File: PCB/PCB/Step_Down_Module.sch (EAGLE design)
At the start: 48 parts, among them J1 JUMPER-SMT_3_1-NC_PASTE_SILK, J2 JUMPER-SMT_3_1-NC_PASTE_SILK, J7 JUMPER-SMT_3_1-NC_PASTE_SILK, Q1 FDMC86240, Q2 FDMC86240, Q3 TPH2900ENH, U1 LTC3895_STEP_DOWN_DC-DC_CONVE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

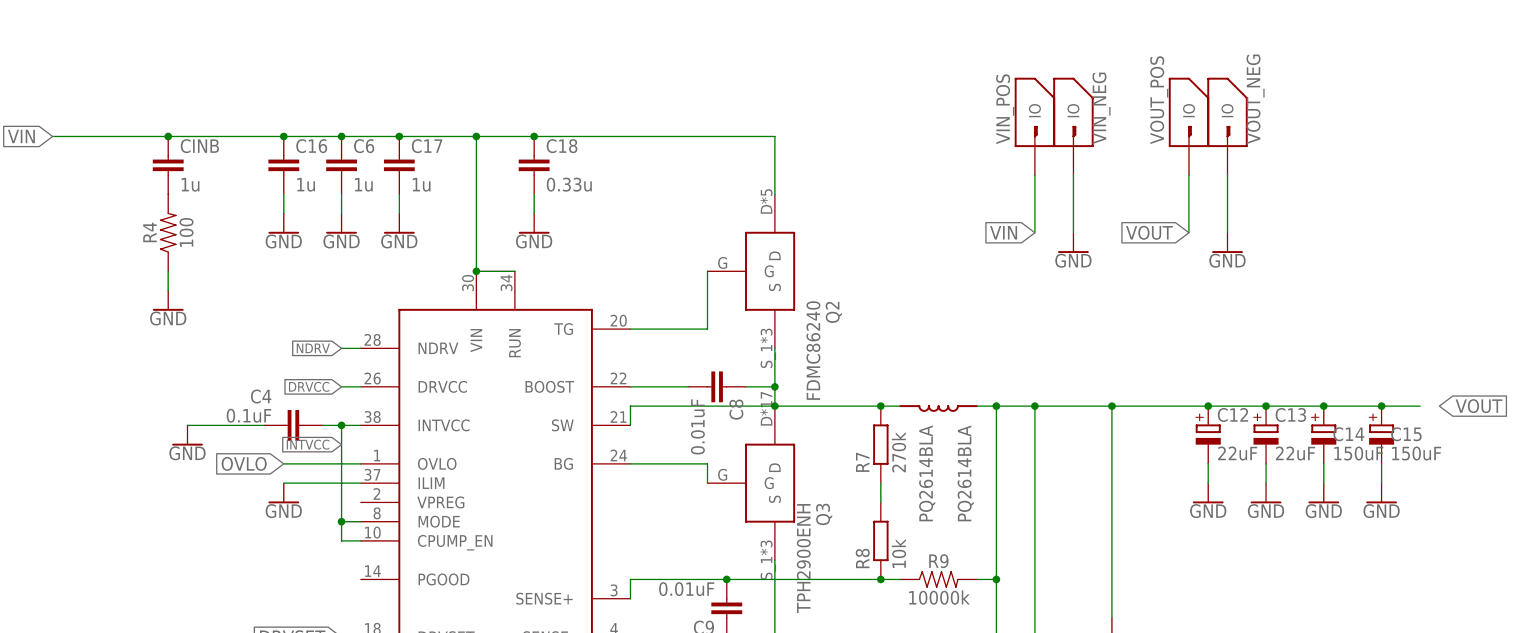
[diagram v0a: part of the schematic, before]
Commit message: WIP-PCB revision 2; Major parts of layout done
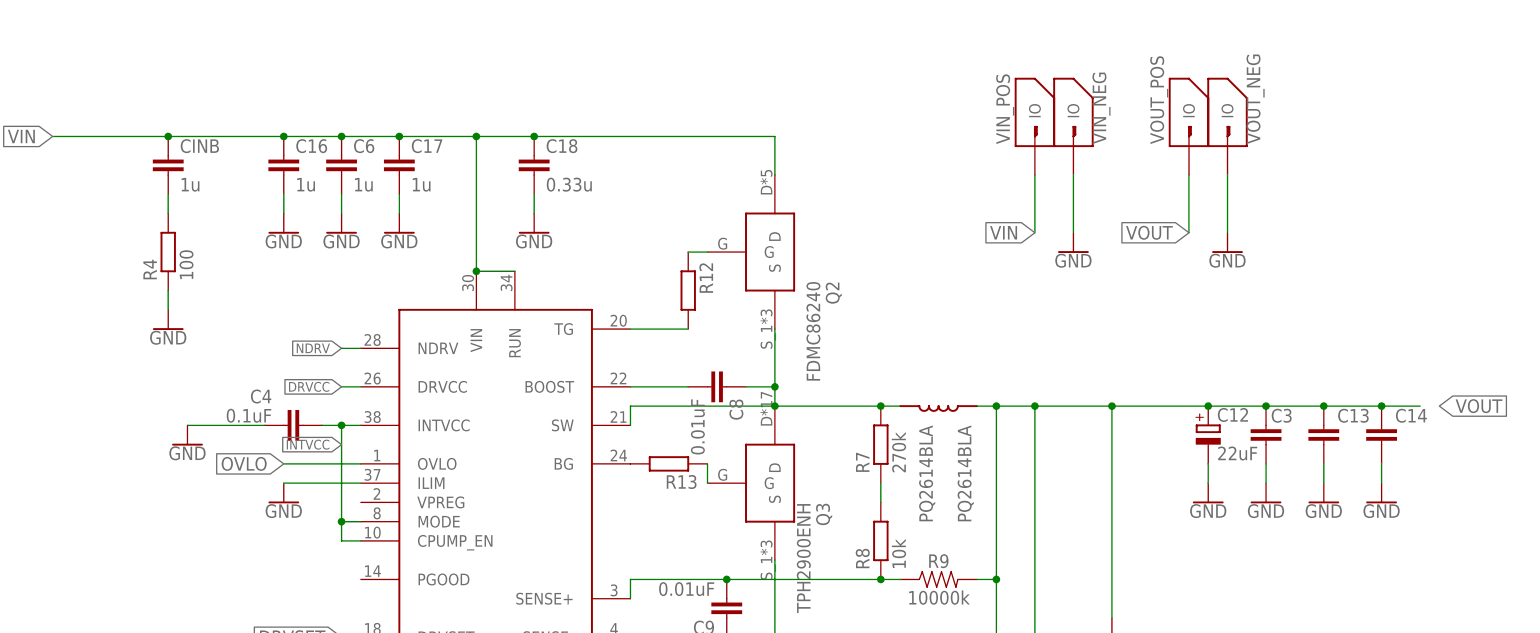
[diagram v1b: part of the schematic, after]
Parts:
- removed C15: 150uF, rcl:CPOL-EUE5-10.5
- added C3: (no value), rcl:C-EUC0805
- added R12, R13: (no value), rcl:R-EU_R0805
- C13: value 22uF -> (none); device rcl:CPOL-EUE5-5 -> rcl:C-EUC0805
- C14: value 150uF -> (none); device rcl:CPOL-EUE5-10.5 -> rcl:C-EUC0805
- R4: device SparkFun-Resistors:RESISTORAXIAL-0.3 -> resistor:R-EU_0204/5
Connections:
- new net N$2: Q2.G, R12.1
- new net N$3: Q3.G, R13.1
- net G2: now also R12.2; no longer Q2.G
- net G3: now also R13.2; no longer Q3.G
- net GND: now also C13.2, C14.2, C3.2; no longer C13.-, C14.-, C15.-
- net VOUT: now also C13.1, C14.1, C3.1; no longer C13.+, C14.+, C15.+
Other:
- moved on the sheet: Q2

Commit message: WIP:PCB revision 2; Move inductor and optimize SW Node area
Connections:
- net N$6 renamed S+
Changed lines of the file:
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@@
 <part name="VIN_POS" library="IO_pad" deviceset="IO_PAD_SINGLE" device=""/>
 <part name="VIN_NEG" library="IO_pad" deviceset="IO_PAD_SINGLE" device=""/>
-<part name="VOUT_POS" library="IO_pad" deviceset="IO_PAD_SINGLE" device=""/>
 <part name="VOUT_NEG" library="IO_pad" deviceset="IO_PAD_SINGLE" device=""/>
 <part name="U$1" library="IO_pad" deviceset="CONN_VIA" device=""/>
@@
 <part name="C13" library="rcl" library_urn="urn:adsk.eagle:library:334" deviceset="C-EU" device="C0805" package3d_urn="urn:adsk.eagle:package:23617/2"/>
 <part name="C14" library="rcl" library_urn="urn:adsk.eagle:library:334" deviceset="C-EU" device="C0805" package3d_urn="urn:adsk.eagle:package:23617/2"/>
+<part name="VOUT_POS" library="IO_pad" deviceset="IO_PAD_SINGLE" device=""/>
 </parts>
 <sheets>
@@
 <attribute name="NAME" x="100.838" y="108.204" size="1.778" layer="95" rot="R90"/>
 </instance>
-<instance part="VOUT_POS" gate="G$1" x="109.22" y="111.76" smashed="yes">
-<attribute name="NAME" x="108.458" y="108.204" size="1.778" layer="95" rot="R90"/>
-</instance>
 <instance part="VOUT_NEG" gate="G$1" x="114.3" y="111.76" smashed="yes">
 <attribute name="NAME" x="121.158" y="108.204" size="1.778" layer="95" rot="R90"/>
@@
 <attribute name="NAME" x="143.256" y="73.279" size="1.778" layer="95" rot="R180"/>
 <attribute name="VALUE" x="139.319" y="72.644" size="1.778" layer="96" rot="R90"/>
+</instance>
+<instance part="VOUT_POS" gate="G$1" x="109.22" y="111.76" smashed="yes">
+<attribute name="NAME" x="108.458" y="108.204" size="1.778" layer="95" rot="R90"/>
 </instance>
 </instances>
@@
 </segment>
 </net>
-<net name="N$6" class="0">
+<net name="S+" class="0">
 <segment>
 <pinref part="U1" gate="G$1" pin="SENSE+"/>

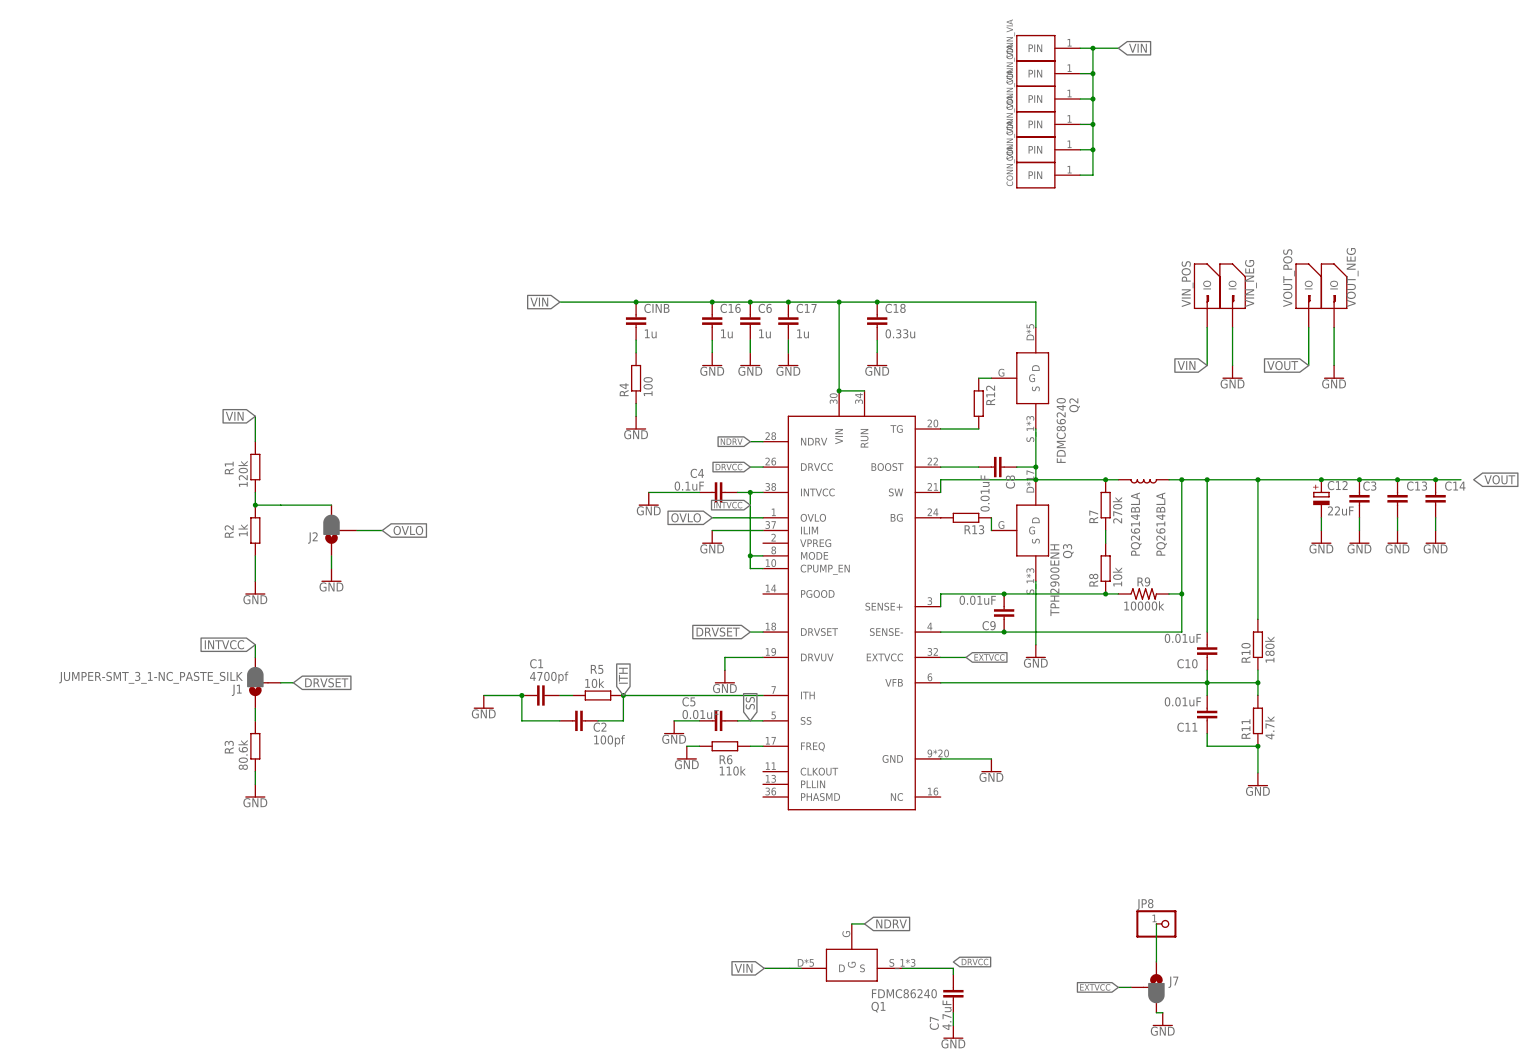
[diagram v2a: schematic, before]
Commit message: Corrected sense resistors, DRVCC trace
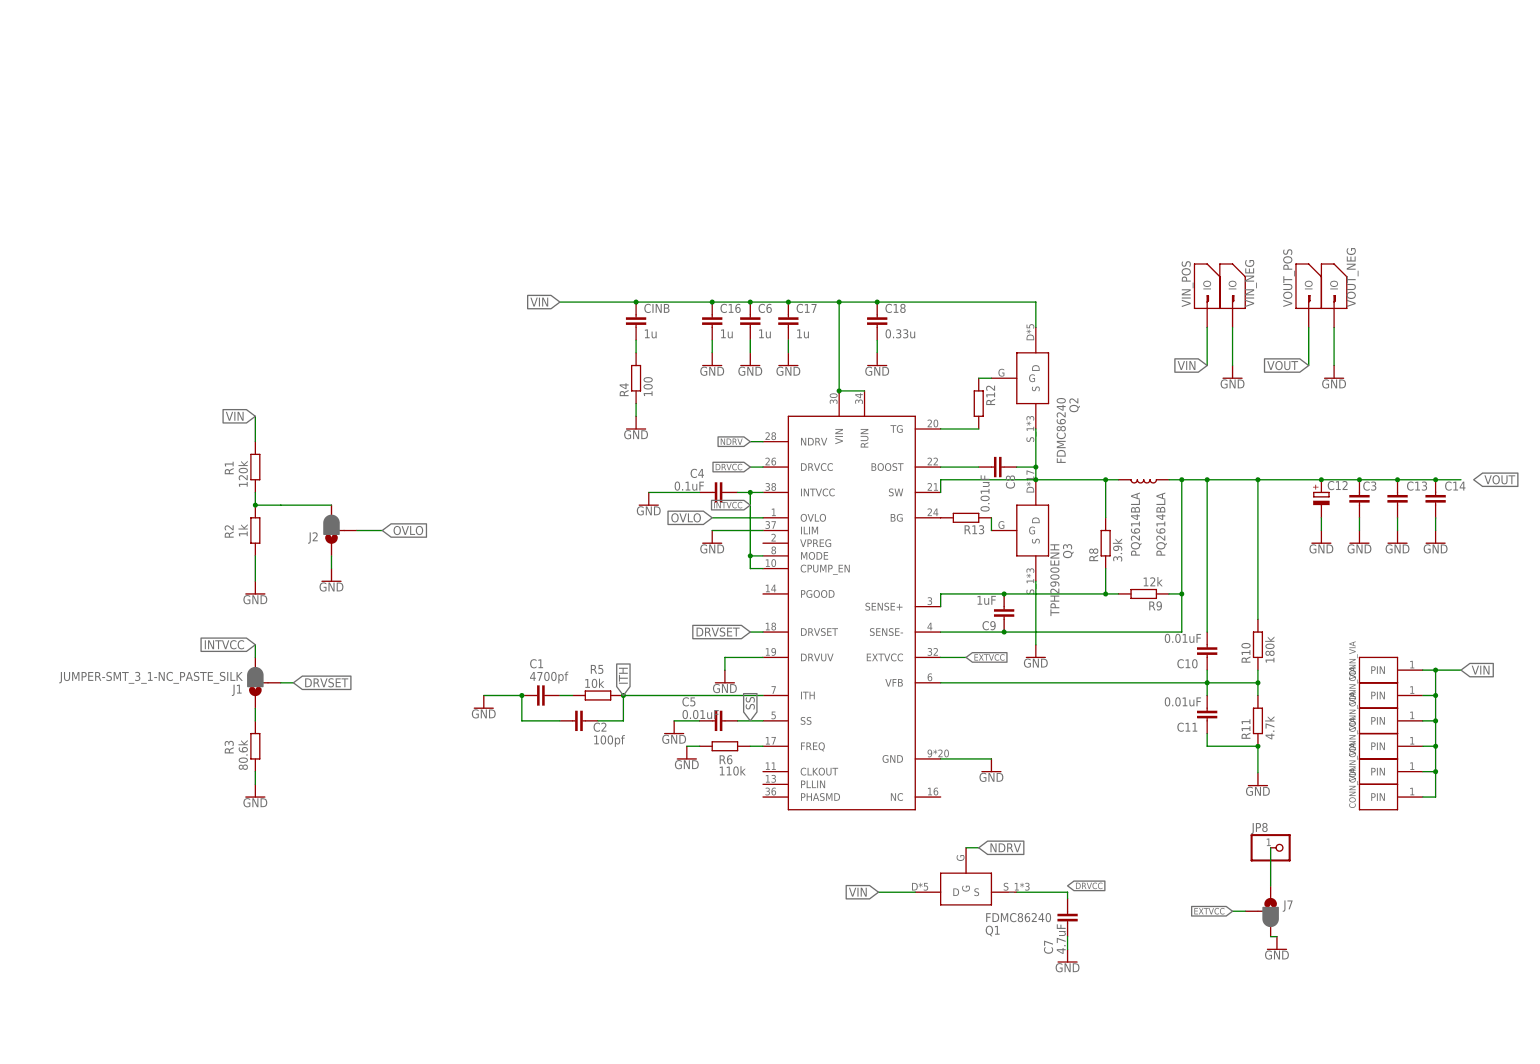
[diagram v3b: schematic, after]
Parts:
- removed R7: 270k, rcl:R-EU_R0805
- C12: value 22uF -> (none)
- C9: value 0.01uF -> 1uF
- R8: value 10k -> 3.9k; device rcl:R-EU_R0805 -> resistor:R-EU_0204/5
- R9: value 10000k -> 12k; device SparkFun-Resistors:RESISTORAXIAL-0.3 -> resistor:R-EU_0204/5
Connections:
- removed net N$7: R7.1, R8.2
- net S+: now also R9.2; no longer R9.1
- net SW: now also R8.2; no longer R7.2
- net VOUT: now also R9.1; no longer R9.2
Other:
- moved on the sheet: C7, J7, JP8, Q1, R8

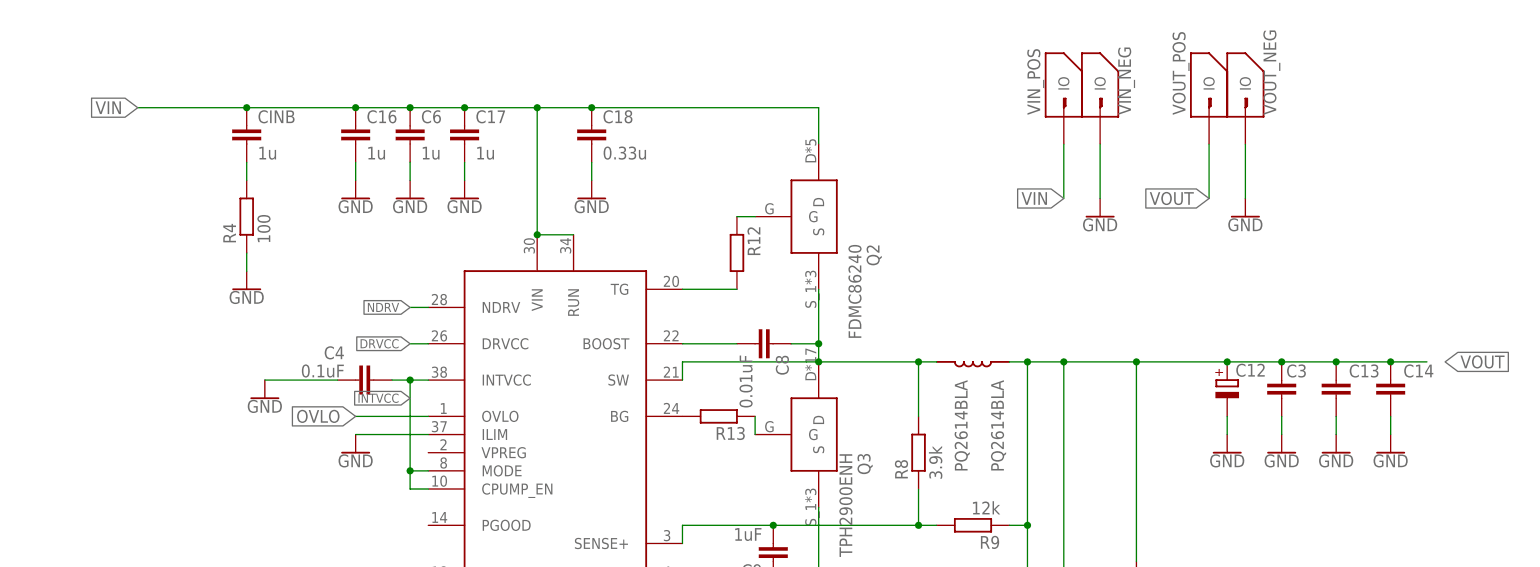
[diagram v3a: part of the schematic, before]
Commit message: Added electrolytics, test points
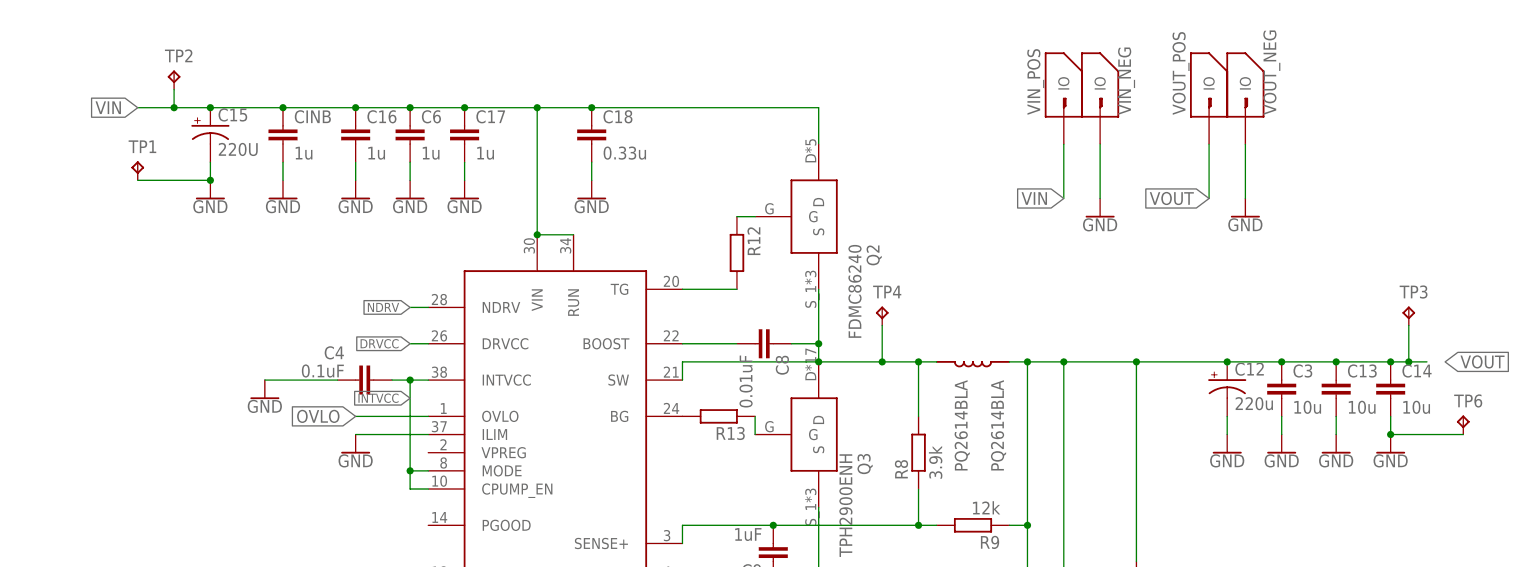
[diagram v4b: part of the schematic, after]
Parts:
- removed R4: 100, resistor:R-EU_0204/5
- added C15: 220U, SparkFun-Capacitors:220U
- added TP1, TP2, TP3, TP4, TP6: TPTP16R, testpad:TPTP16R
- C12: value (none) -> 220u; device rcl:CPOL-EUE5-5 -> SparkFun-Capacitors:1000UF-RADIAL-5MM-25V-20%
- C13, C14, C3: value (none) -> 10u; device rcl:C-EUC0805 -> SparkFun-Capacitors:CAP_SMD_1210
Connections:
- removed net N$1: CINB.2, R4.2
- net GND: now also C15.-, CINB.2, TP1.TP, TP6.TP; no longer R4.1
- net SW: now also TP4.TP
- net VIN: now also C15.+, TP2.TP
- net VOUT: now also TP3.TP
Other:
- moved on the sheet: CINB

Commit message: PCB rev2 sent for manufacture
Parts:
- added C19: 10u, SparkFun-Capacitors:CAP_SMD_1210
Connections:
- net GND: now also C19.2
- net VOUT: now also C19.1
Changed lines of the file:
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@@
 <part name="TP4" library="testpad" library_urn="urn:adsk.eagle:library:385" deviceset="TP" device="TP16R" package3d_urn="urn:adsk.eagle:package:27969/1"/>
 <part name="TP6" library="testpad" library_urn="urn:adsk.eagle:library:385" deviceset="TP" device="TP16R" package3d_urn="urn:adsk.eagle:package:27969/1"/>
+<part name="C19" library="SparkFun-Capacitors" deviceset="CAP_SMD_1210" device="" value="10u"/>
+<part name="GND28" library="SparkFun-PowerSymbols" library_urn="urn:adsk.eagle:library:530" deviceset="GND" device=""/>
 </parts>
 <sheets>
@@
 <attribute name="NAME" x="146.05" y="67.31" size="1.778" layer="95"/>
 <attribute name="TP_SIGNAL_NAME" x="148.59" y="64.77" size="1.778" layer="97"/>
+</instance>
+<instance part="C19" gate="G$1" x="121.92" y="78.74" smashed="yes" rot="R180">
+<attribute name="NAME" x="120.396" y="75.819" size="1.778" layer="95" font="vector" rot="R180"/>
+<attribute name="VALUE" x="120.396" y="80.899" size="1.778" layer="96" font="vector" rot="R180"/>
+</instance>
+<instance part="GND28" gate="1" x="121.92" y="86.36" smashed="yes" rot="R180">
+<attribute name="VALUE" x="121.92" y="86.614" size="1.778" layer="96" rot="R180" align="top-center"/>
 </instance>
 </instances>
@@
 <wire x1="139.7" y1="78.74" x2="139.7" y2="73.66" width="0.1524" layer="91"/>
 <junction x="139.7" y="73.66"/>
+<pinref part="C19" gate="G$1" pin="1"/>
 </segment>
 <segment>
@@
 <junction x="-27.94" y="99.06"/>
 </segment>
-</net>
+<segment>
+<pinref part="C19" gate="G$1" pin="2"/>
+<pinref part="GND28" gate="1" pin="GND"/>
+<wire x1="121.92" y1="83.82" x2="121.92" y2="81.28" width="0.1524" layer="91"/>
+</segment>
+</net>
